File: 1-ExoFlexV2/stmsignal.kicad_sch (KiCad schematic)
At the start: 4 parts, among them J10 CN9, J11 CN7, J12 CN10, J9 CN8

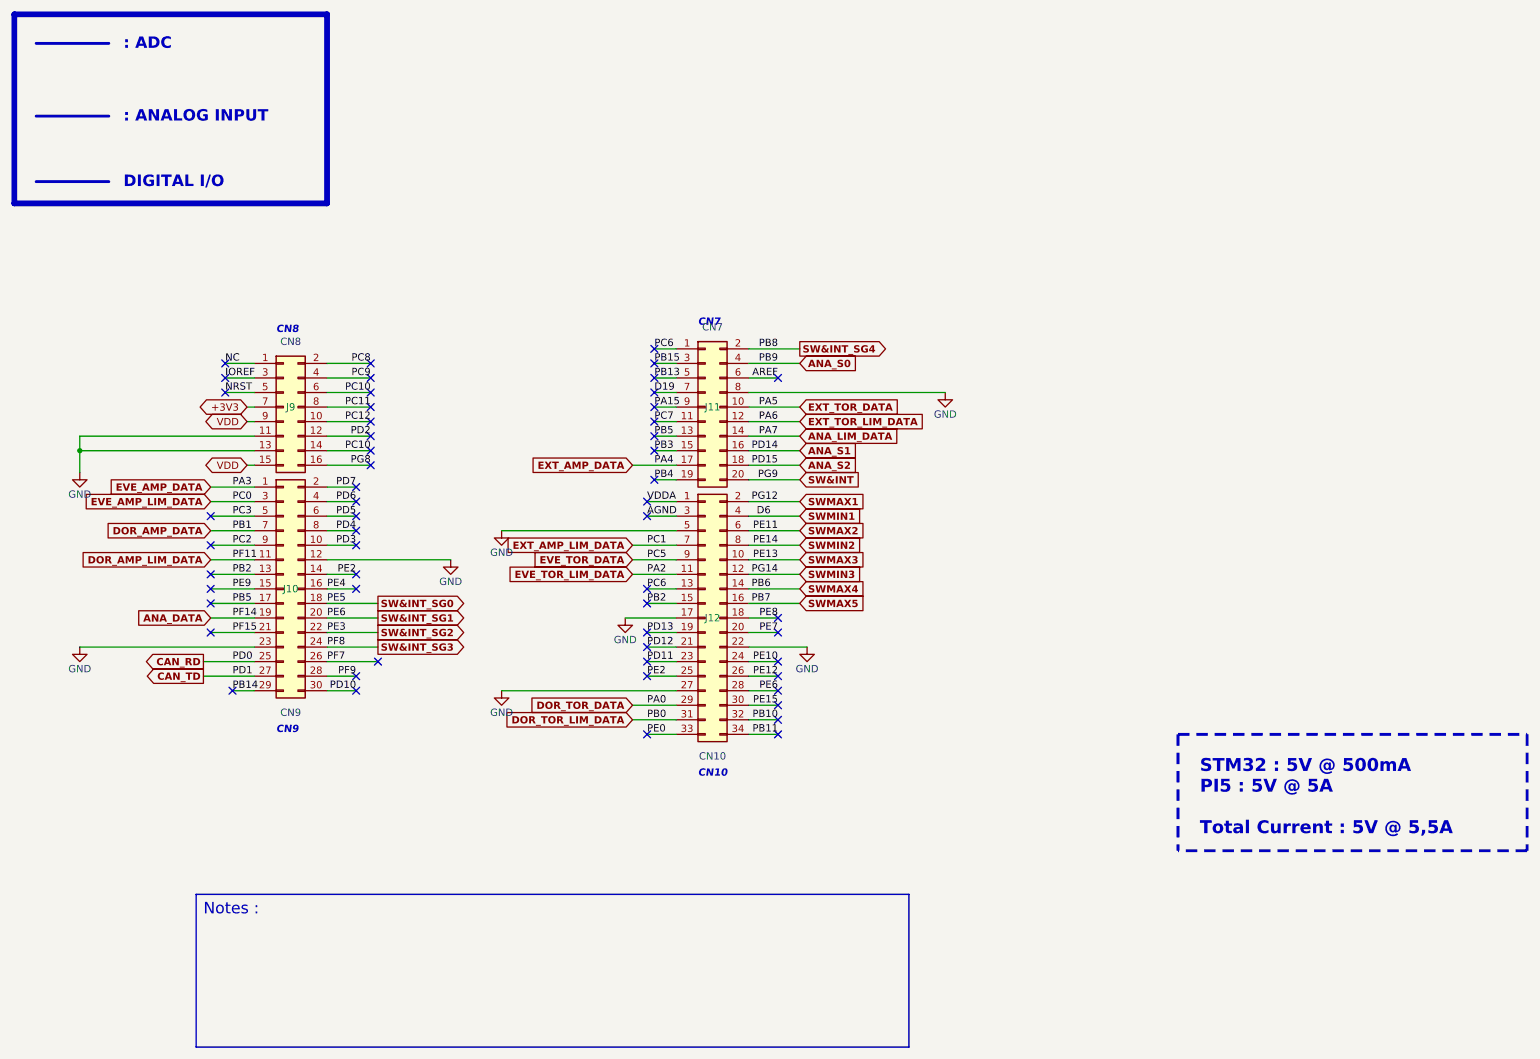
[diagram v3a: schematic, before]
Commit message: Bug NetList
- Ajout de net-tie pour les GND et et les +5V
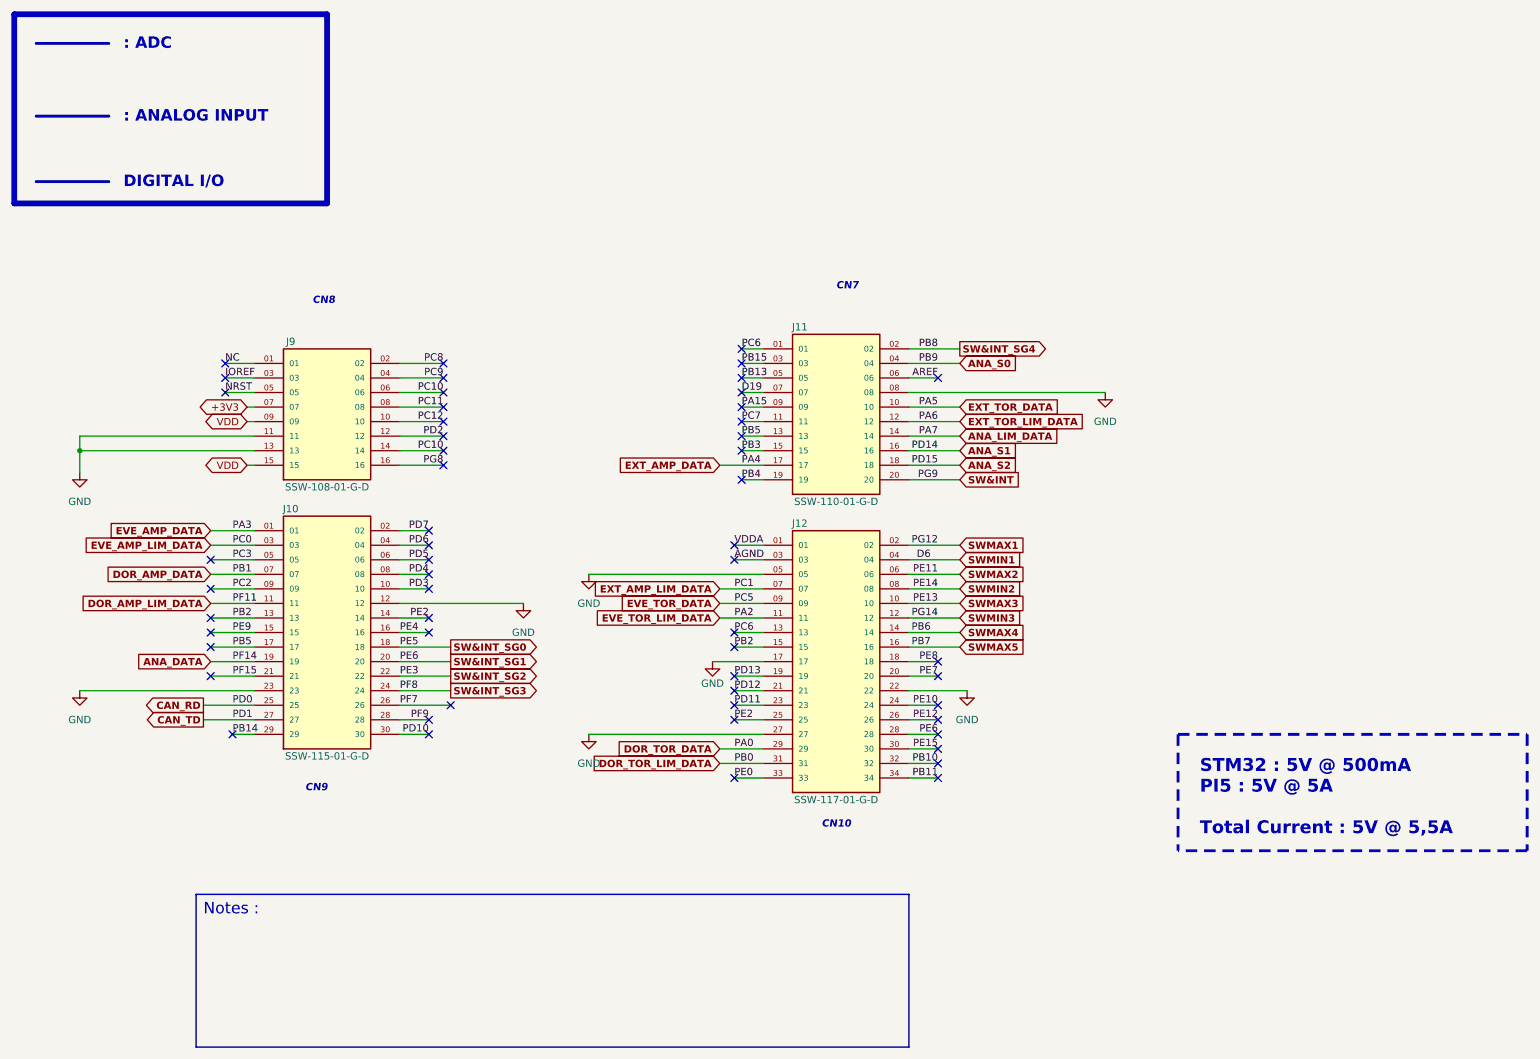
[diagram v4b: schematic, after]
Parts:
- removed J10: CN9, FootPrintLib:SAMTEC_SSW-115-01-G-D, symbol Connector_Generic:Conn_02x15_Odd_Even
- removed J11: CN7, FootPrintLib:SAMTEC_SSW-110-01-G-D, symbol Connector_Generic:Conn_02x10_Odd_Even
- removed J12: CN10, FootPrintLib:SAMTEC_SSW-117-01-G-D, symbol Connector_Generic:Conn_02x17_Odd_Even
- removed J9: CN8, FootPrintLib:SAMTEC_SSW-108-01-G-D, symbol Connector_Generic:Conn_02x08_Odd_Even
- added J10: SSW-115-01-G-D, FootPrintLib:SAMTEC_SSW-115-01-G-D, symbol SymLib:SSW-115-01-G-D
- added J11: SSW-110-01-G-D, FootPrintLib:SAMTEC_SSW-110-01-G-D, symbol SymLib:SSW-110-01-G-D
- added J12: SSW-117-01-G-D, FootPrintLib:SAMTEC_SSW-117-01-G-D, symbol SymLib:SSW-117-01-G-D
- added J9: SSW-108-01-G-D, FootPrintLib:SAMTEC_SSW-108-01-G-D, symbol SymLib:SSW-108-01-G-D
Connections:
- net +3V3: now also J9.07
- net AGND: now also J12.03
- net ANA_DATA: now also J10.19
- net ANA_LIM_DATA: now also J11.14
- net ANA_S0: now also J11.04
- net ANA_S1: now also J11.16
- net ANA_S2: now also J11.18
- net AREF: now also J11.06
- net CAN_RD: now also J10.25
- net CAN_TD: now also J10.27
- net D19: now also J11.07
- net DOR_AMP_DATA: now also J10.07
- net DOR_AMP_LIM_DATA: now also J10.11
- net DOR_TOR_DATA: now also J12.29
- net DOR_TOR_LIM_DATA: now also J12.31
- net EVE_AMP_DATA: now also J10.01
- net EVE_AMP_LIM_DATA: now also J10.03
- net EVE_TOR_DATA: now also J12.09
- net EVE_TOR_LIM_DATA: now also J12.11
- net EXT_AMP_DATA: now also J11.17
- net EXT_AMP_LIM_DATA: now also J12.07
- net EXT_TOR_DATA: now also J11.10
- net EXT_TOR_LIM_DATA: now also J11.12
- net GND: now also J10.12, J10.23, J11.08, J12.05, J12.17, J12.22, J12.27, J9.11, J9.13
- net IOREF: now also J9.03
- net NC: now also J9.01
- net NRST: now also J9.05
- net PA15: now also J11.09
- net PB10: now also J12.32
- net PB11: now also J12.34
- net PB13: now also J11.05
- net PB14: now also J10.29
- net PB15: now also J11.03
- net PB2: now also J10.13, J12.15
- net PB3: now also J11.15
- net PB4: now also J11.19
- net PB5: now also J10.17, J11.13
- net PC10: now also J9.06, J9.14
- net PC11: now also J9.08
- net PC12: now also J9.10
- net PC2: now also J10.09
- net PC3: now also J10.05
- net PC6: now also J11.01, J12.13
- net PC7: now also J11.11
- net PC8: now also J9.02
- net PC9: now also J9.04
- net PD10: now also J10.30
- net PD11: now also J12.23
- net PD12: now also J12.21
- net PD13: now also J12.19
- net PD2: now also J9.12
- net PD3: now also J10.10
- net PD4: now also J10.08
- net PD5: now also J10.06
- net PD6: now also J10.04
- net PD7: now also J10.02
- net PE0: now also J12.33
- net PE10: now also J12.24
- net PE12: now also J12.26
- net PE15: now also J12.30
- net PE2: now also J10.14, J12.25
- net PE4: now also J10.16
- net PE7: now also J12.20
- net PE8: now also J12.18
- net PE9: now also J10.15
- net PF15: now also J10.21
- net PF7: now also J10.26
- net PF9: now also J10.28
- net PG8: now also J9.16
- net SW&INT: now also J11.20
- net SW&INT_SG0: now also J10.18
- net SW&INT_SG1: now also J10.20, J12.28
- net SW&INT_SG2: now also J10.22
- net SW&INT_SG3: now also J10.24
- net SW&INT_SG4: now also J11.02
- net SWMAX1: now also J12.02
- net SWMAX2: now also J12.06
- net SWMAX3: now also J12.10
- net SWMAX4: now also J12.14
- net SWMAX5: now also J12.16
- net SWMIN1: now also J12.04
- net SWMIN2: now also J12.08
- net SWMIN3: now also J12.12
- net VDD: now also J9.09, J9.15
- net VDDA: now also J12.01

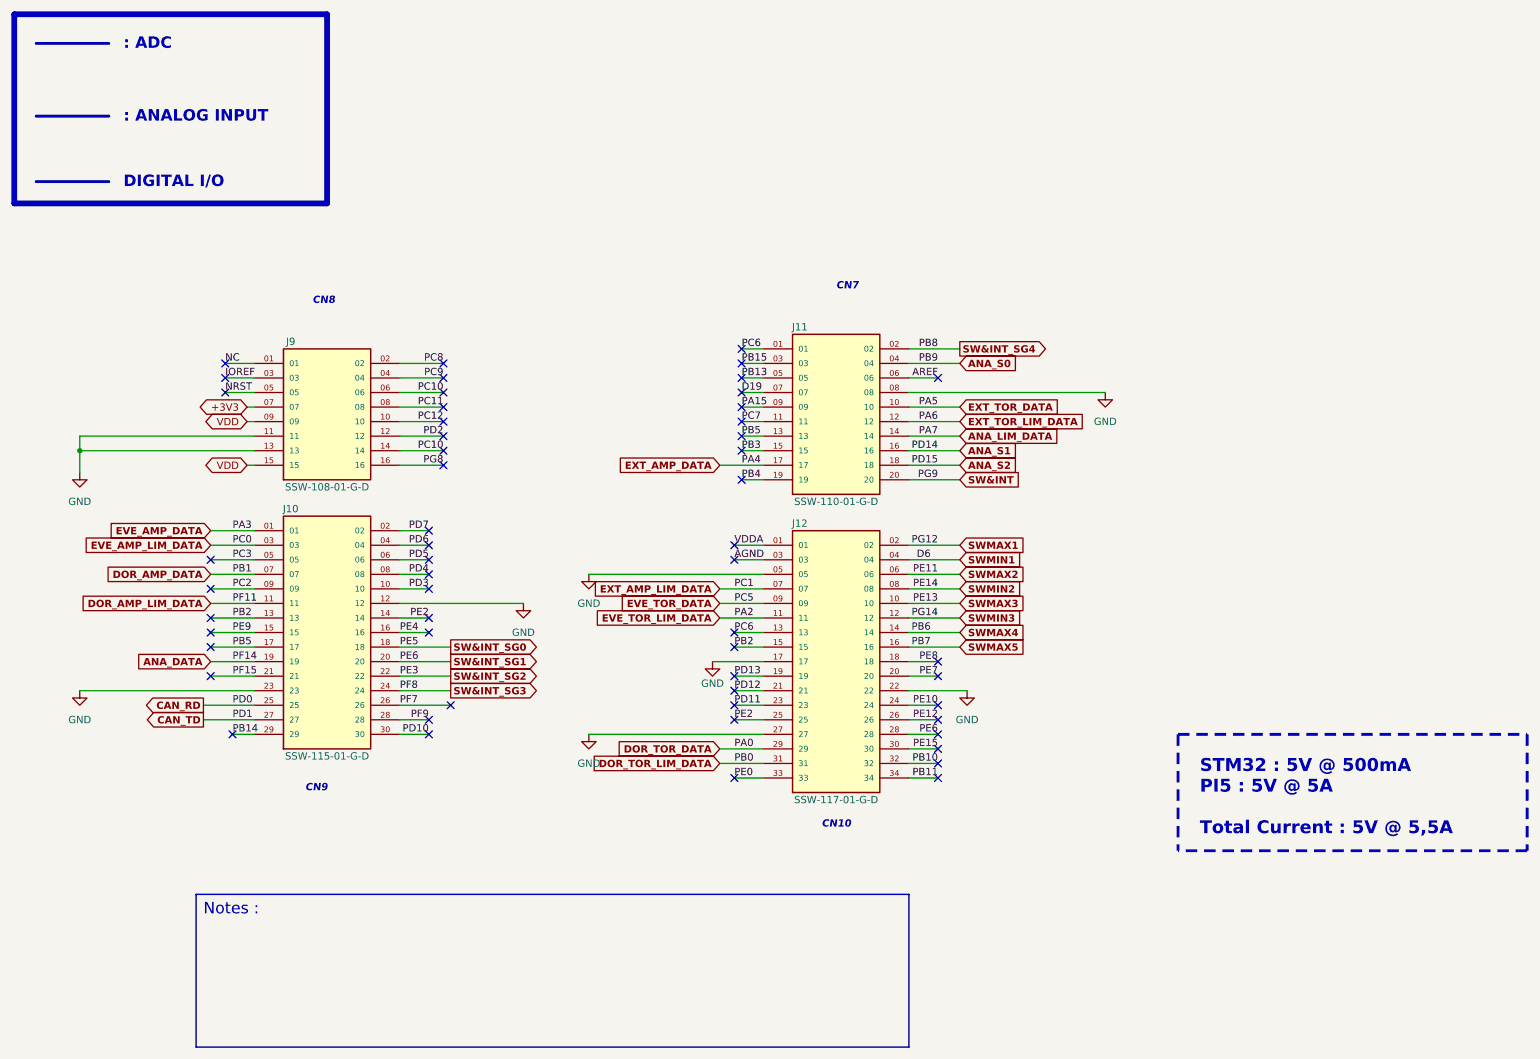
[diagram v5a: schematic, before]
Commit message: Finalisation schéma FIN
- Changement des uméro pour les inverseurs
- Changement des connecteur et début de placement
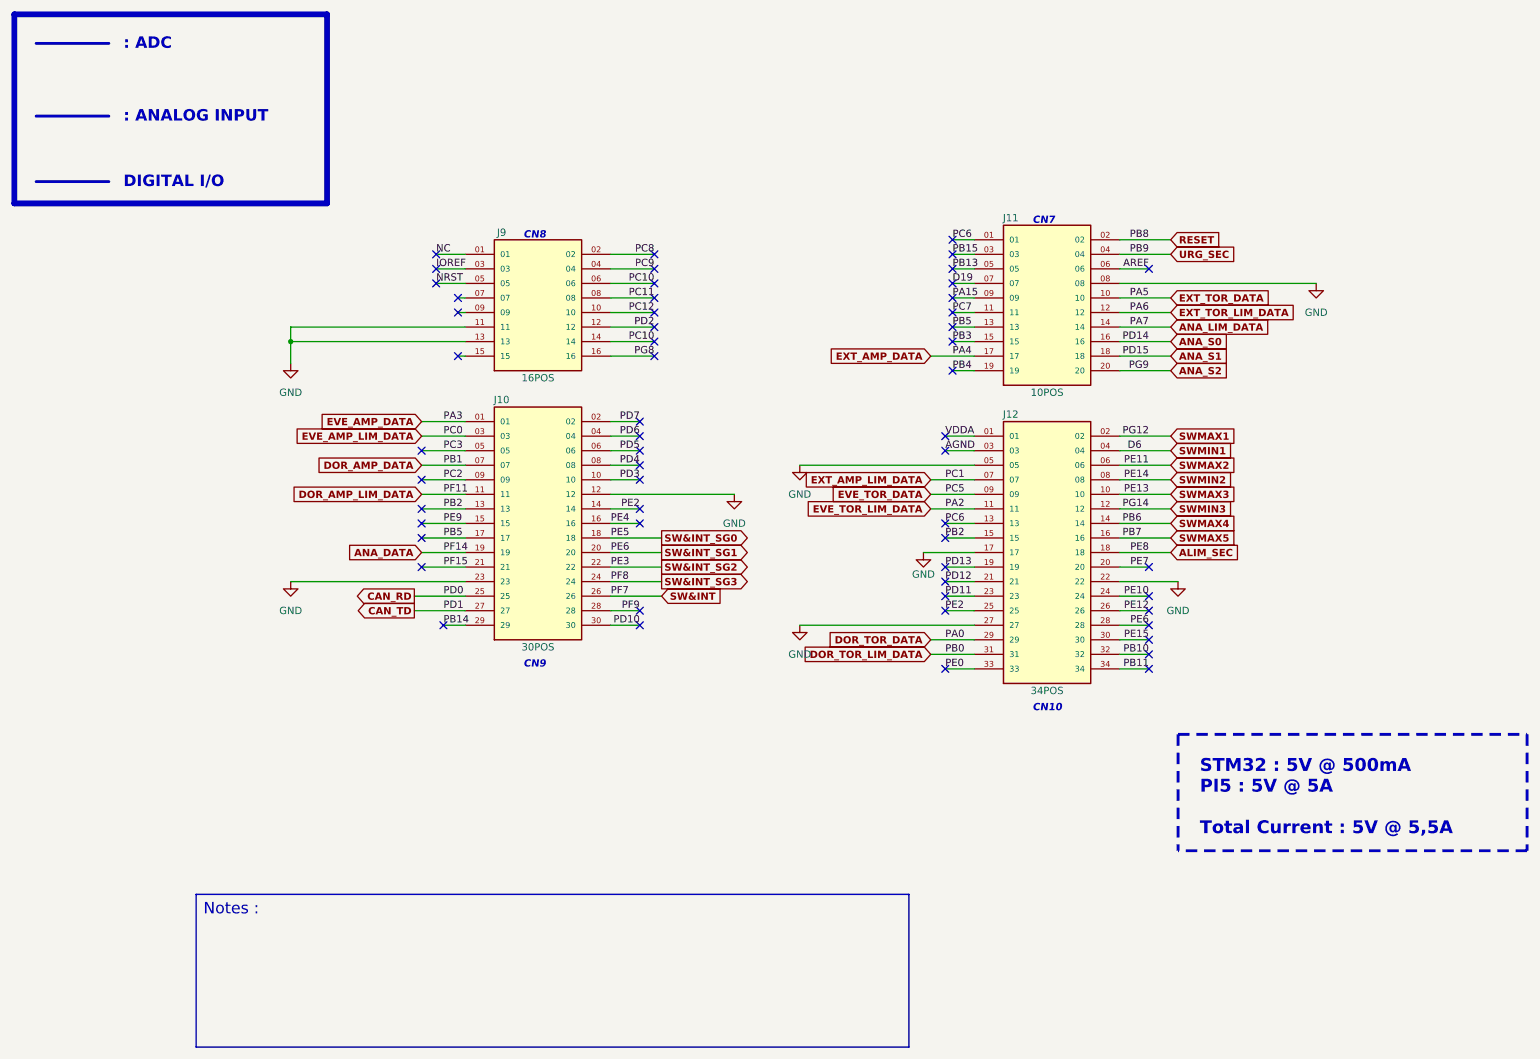
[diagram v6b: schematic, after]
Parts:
- J10: value SSW-115-01-G-D -> 30POS; DESCRIPTION (none) -> 30 Position Receptacle Connector 0.100" (2.54mm) Through Ho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; MANUFACTURER Samtec -> Samtec Inc.; PART NUMBER (none) -> SSW-115-01-G-D
- J11: value SSW-110-01-G-D -> 10POS; DESCRIPTION (none) -> 20 Position Receptacle Connector 0.100" (2.54mm) Through Ho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; PART NUMBER (none) -> SSW-110-01-G-D
- J12: value SSW-117-01-G-D -> 34POS; DESCRIPTION (none) -> 34 Position Receptacle Connector 0.100" (2.54mm) Through Ho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; MANUFACTURER Samtec -> Samtec Inc.; PART NUMBER (none) -> SSW-117-01-G-D
- J9: value SSW-108-01-G-D -> 16POS; DESCRIPTION (none) -> 16 Position Receptacle Connector 0.100" (2.54mm) Through Ho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; MANUFACTURER Samtec -> Samtec Inc.; PART NUMBER (none) -> SSW-108-01-G-D
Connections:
- net PF7 is gone; now on net SW&INT: J10.26
- net ANA_S0: now also J11.16; no longer J11.04
- net ANA_S1: now also J11.18; no longer J11.16
- net ANA_S2: now also J11.20; no longer J11.18
- net SW&INT: no longer J11.20
- net +3V3: no longer names the net of J9.07
- net PE8 renamed ALIM_SEC
- net SW&INT_SG4 renamed RESET
- net VDD: no longer names the net of J9.09
- net VDD: no longer J9.15
- new net URG_SEC: J11.04
- no-connect marks 55 -> 56
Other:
- moved on the sheet: J10, J11, J12, J9

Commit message: Routage 3
- Routage des connecteurs terminé
- Routage des signaux terminé
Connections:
- net PB2: no longer J12.15
- net PC10: no longer J9.14
- net PE2: no longer J12.25
- net SW&INT_SG1: no longer J12.28
- new net PPB2: J12.15
- new net PPC10: J9.14
- new net PPE2: J12.25
- new net PPE6: J12.28
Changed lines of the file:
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@@
     (effects (font (size 1.27 1.27)) (justify left bottom))
   )
-  (label "PC10" (at 128.27 72.39 180)
+  (label "PPC10" (at 128.27 72.39 180)
     (effects (font (size 1.27 1.27)) (justify right bottom))
   )
-  (label "PE6" (at 214.63 121.92 180)
+  (label "PPE6" (at 214.63 121.92 180)
     (effects (font (size 1.27 1.27)) (justify right bottom))
   )
@@
     (effects (font (size 1.27 1.27)) (justify right bottom))
   )
-  (label "PB2" (at 179.07 106.68 0)
+  (label "PPB2" (at 179.07 106.68 0)
     (effects (font (size 1.27 1.27)) (justify left bottom))
   )
@@
     (effects (font (size 1.27 1.27)) (justify left bottom))
   )
-  (label "PE2" (at 179.07 119.38 0)
+  (label "PPE2" (at 179.07 119.38 0)
     (effects (font (size 1.27 1.27)) (justify left bottom))
   )

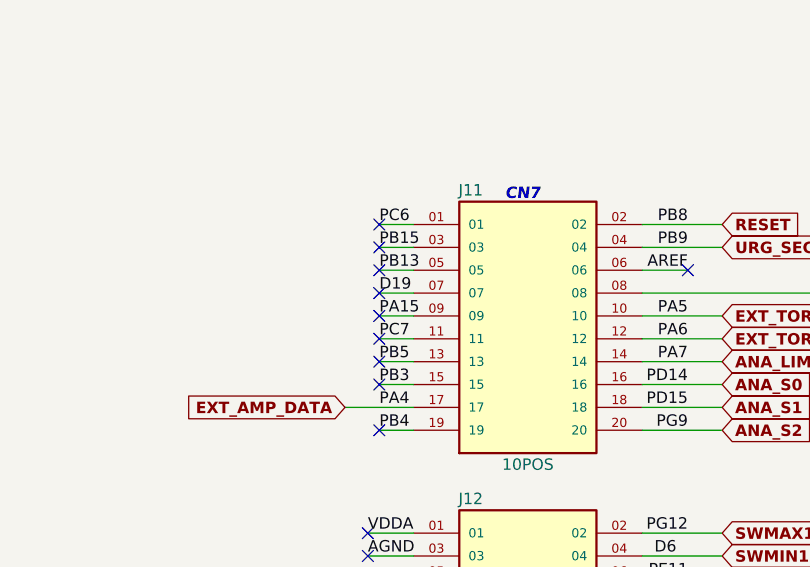
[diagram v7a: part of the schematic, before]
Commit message: Routage Fin
- Alimentation router
- Urg Sec dans le OR gate vers Alim Sec
- Changement d'un condo
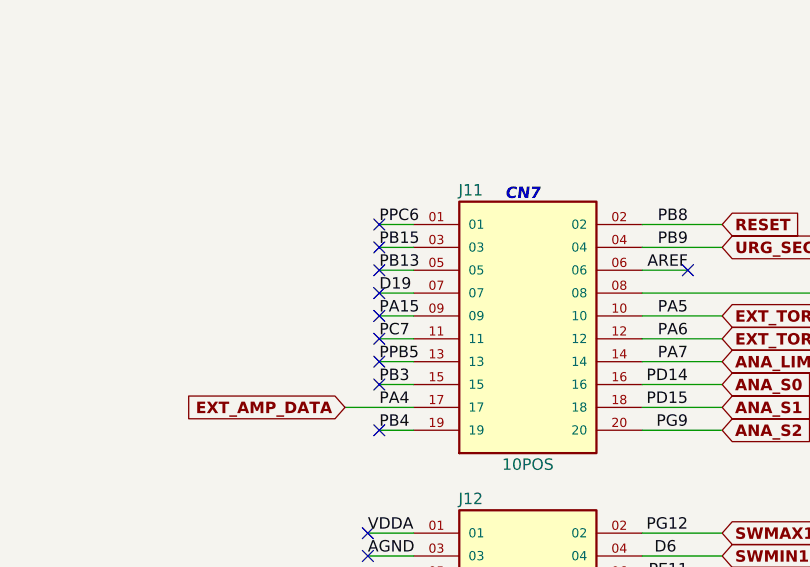
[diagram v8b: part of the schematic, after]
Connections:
- net PB5: no longer J11.13
- net PC6: no longer J11.01
- new net PPB5: J11.13
- new net PPC6: J11.01
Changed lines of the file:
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@@
     (effects (font (size 1.27 1.27)) (justify left bottom))
   )
-  (label "PB5" (at 180.34 69.85 0)
+  (label "PPB5" (at 180.34 69.85 0)
     (effects (font (size 1.27 1.27)) (justify left bottom))
   )
@@
     (effects (font (size 1.27 1.27)) (justify right bottom))
   )
-  (label "PC6" (at 180.34 54.61 0)
+  (label "PPC6" (at 180.34 54.61 0)
     (effects (font (size 1.27 1.27)) (justify left bottom))
   )
